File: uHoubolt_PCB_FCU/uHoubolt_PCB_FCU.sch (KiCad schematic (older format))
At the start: 0 parts

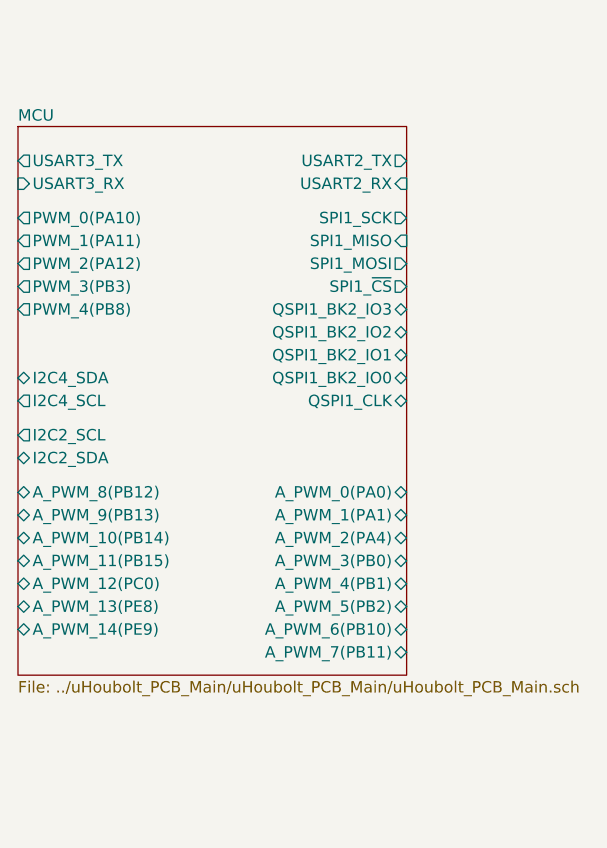
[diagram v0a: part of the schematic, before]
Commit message: add power symbols
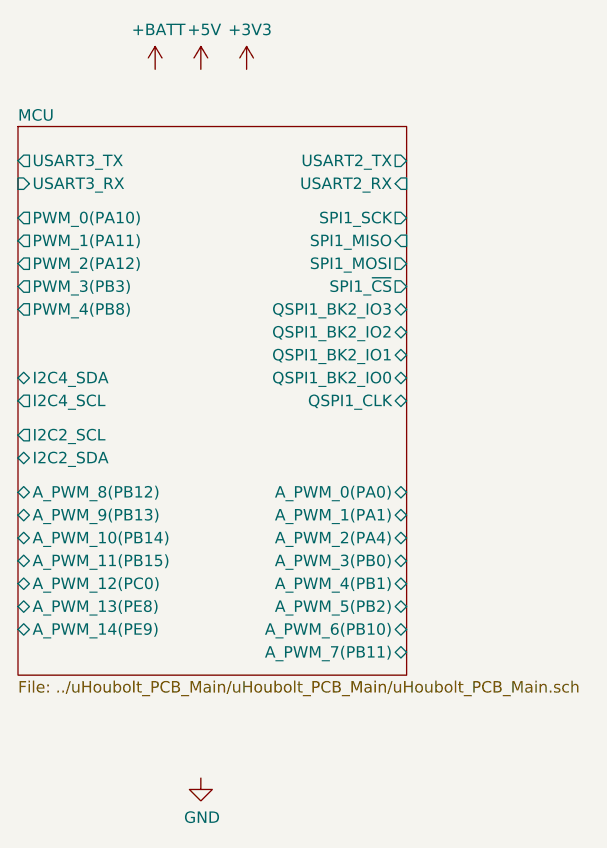
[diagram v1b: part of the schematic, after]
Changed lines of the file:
@@
 F38 "PWM_4(PB8)" O L 4050 3300 50
 $EndSheet
+$Comp
+L power:+BATT #PWR?
+U 1 1 5FDDCBBE
+P 4650 2250
+F 0 "#PWR?" H 4650 2100 50  0001 C CNN
+F 1 "+BATT" H 4665 2423 50  0000 C CNN
+F 2 "" H 4650 2250 50  0001 C CNN
+F 3 "" H 4650 2250 50  0001 C CNN
+	1    4650 2250
+	1    0    0    -1
+$EndComp
+$Comp
+L power:+5V #PWR?
+U 1 1 5FDDCF04
+P 4850 2250
+F 0 "#PWR?" H 4850 2100 50  0001 C CNN
+F 1 "+5V" H 4865 2423 50  0000 C CNN
+F 2 "" H 4850 2250 50  0001 C CNN
+F 3 "" H 4850 2250 50  0001 C CNN
+	1    4850 2250
+	1    0    0    -1
+$EndComp
+$Comp
+L power:+3V3 #PWR?
+U 1 1 5FDDD390
+P 5050 2250
+F 0 "#PWR?" H 5050 2100 50  0001 C CNN
+F 1 "+3V3" H 5065 2423 50  0000 C CNN
+F 2 "" H 5050 2250 50  0001 C CNN
+F 3 "" H 5050 2250 50  0001 C CNN
+	1    5050 2250
+	1    0    0    -1
+$EndComp
+$Comp
+L power:GND #PWR?
+U 1 1 5FDDDF58
+P 4850 5350
+F 0 "#PWR?" H 4850 5100 50  0001 C CNN
+F 1 "GND" H 4855 5177 50  0000 C CNN
+F 2 "" H 4850 5350 50  0001 C CNN
+F 3 "" H 4850 5350 50  0001 C CNN
+	1    4850 5350
+	1    0    0    -1
+$EndComp
 $EndSCHEMATC

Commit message: add 10A solenoid circuit
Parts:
- added C1, C?: 0.1u, symbol Device:C_Small
- added J1, J?: 206832-0202, symbol Connector_Generic:Conn_01x02
- added Q1, Q?: BUK9M15-40H, Package_TO_SOT_SMD:LFPAK33, symbol Transistor_FET:BUK9M15-60EX
- added R1, R?: shunt, symbol Device:R_Small
- added R2, R?: 20k, symbol Device:R_Small
- added R3, R?: 200, symbol Device:R_Small
- added U1, U?: INA180, Package_TO_SOT_SMD:SOT-23-6, symbol TXV_LIB:INA180
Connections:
- net labels added: SOLCONTROL1, SOLCONTROL2, SOLSENSE1, SOLSENSE2
- wire segments 0 -> 56

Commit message: add 5V Zünder circuit
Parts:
- removed Q1, Q?: BUK9M15-40H, Package_TO_SOT_SMD:LFPAK33, symbol Transistor_FET:BUK9M15-60EX
- added C3, C4: 0.1u, symbol Device:C_Small
- added J3, J4: 206832-0202, symbol Connector_Generic:Conn_01x02
- added Q1, Q2, Q3, Q4: BSB008NE2LX, Package_DirectFET:DirectFET_MX, symbol Transistor_FET:BSB008NE2LX
- added R10, R7: shunt, symbol Device:R_Small
- added R11, R8: 20k, symbol Device:R_Small
- added R12, R9: 200, symbol Device:R_Small
- added U3, U4: INA180, Package_TO_SOT_SMD:SOT-23-6, symbol TXV_LIB:INA180
- gave numbers to parts that had none: 6
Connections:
- net labels added: SERVOCONTROL1, SERVOCONTROL2, SERVOSENSE1, SERVOSENSE2
- wire segments 56 -> 112
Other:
- moved on the sheet: C1, C2, J1, J2, R1, R2, R3, R4, R5, R6, U1, U2

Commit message: add continuity sense to 5V Zünder circuit
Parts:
- added R13: 20k, symbol Device:R_Small
- added R14: 200, symbol Device:R_Small
- added R15: 560k, symbol Device:R_Small
- added R16: 2.0M, symbol Device:R_Small
- R10: value shunt -> 560k
- R11: value 20k -> 2.0M
- R12: value 200 -> shunt
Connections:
- net GND: now also R12.2, R13.1, R15.2; no longer R11.1
- net at J3.2 (Pin_2), Q3.1 (D): now also R11.1
- net at Q4.2 (G): now also R14.2; no longer R12.2
- net at Q4.3 (S), U4.3 (+): now also R12.1; no longer R10.1
- net at J4.2 (Pin_2), Q4.1 (D): now also R16.1
- net SERVOCONTROL1 renamed IGNITECONTROL1
- net SERVOCONTROL2 renamed IGNITECONTINUITY1
- net IGNITECONTINUITY1: now also R10.1; no longer R12.1
- net SERVOSENSE1 renamed IGNITESENSE1
- net SERVOSENSE2 renamed IGNITESENSE2
- new net IGNITECONTINUITY2: R15.1, R16.2
- new net IGNITECONTROL2: R13.2, R14.1
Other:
- moved on the sheet: J3, R8, R9

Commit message: add 2x variable input pressure sensor circuit
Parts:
- added C? (x2): 0.1u, symbol Device:C_Small
- added J? (x2): JST GH, symbol Connector_Generic_MountingPin:Conn_01x04_MountingPin
- added JP?: SolderJumper_3_Open, symbol Jumper:SolderJumper_3_Open
- added R?: 3.3k, symbol Device:R_Small
- added R?: 6.8k, symbol Device:R_Small
- added R? (x2): 3.3k/0, symbol Device:R_Small
- added R? (x2): 6.8k/160, symbol Device:R_Small
- added U? (x2): INA180, Package_TO_SOT_SMD:SOT-23-6, symbol TXV_LIB:INA180
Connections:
- net +3V3: now also C1.1, C2.1, C3.1, C4.1, U1.6 (V+), U2.6 (V+), U3.6 (V+), U4.6 (V+), C?.1, C?.1, U?.6 (V+), U?.6 (V+)
- net +5V: now also JP?.1 (A), R?.1; no longer C1.1, C2.1, C3.1, C4.1, U1.6 (V+), U2.6 (V+), U3.6 (V+), U4.6 (V+)
- net +BATT: now also JP?.3 (B)
- net GND: now also C?.2, C?.2, J?.4 (Pin_4), J?.4 (Pin_4), J?.MP (MountPin), J?.MP (MountPin), R?.2, R?.2, R?.2, U?.2 (GND), U?.2 (GND)
- new net: J?.1 (Pin_1), JP?.2 (C)
- new net: J?.2 (Pin_2), R?.1, U?.3 (+) (x2)
- new net: J?.3 (Pin_3), U?.4 (-) (x2)
- new net PRESSURESENSE2: R?.1, R?.2, U?.1
- new net SUPPLYMEASURE: R?.1, R?.2
- new net TESTPRESSURESENSE1: R?.1, R?.2, U?.1
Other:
- note added: "Vdrive - pyro voltage from PMU\n"
- note added: "op-amp for diff. 150mV bridge input,\nvoltage div. for 0-5V or 4-20mA input.\n(3.3k/6.8k for 0-5V,\n0/160 Ohm for 4-20mA)"
- moved on the sheet: C3, C4, J3, J4, Q3, Q4, R10, R11, R12, R13, R14, R15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

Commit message: Added modules from Trello list. Todo: Review, assign pins to labels, component naming.
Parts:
- removed C4, C?: 0.1u, symbol Device:C_Small
- removed J4: 206832-0202, symbol Connector_Generic:Conn_01x02
- removed J?: JST GH, symbol Connector_Generic_MountingPin:Conn_01x04_MountingPin
- removed Q4: BSB008NE2LX, Package_DirectFET:DirectFET_MX, symbol Transistor_FET:BSB008NE2LX
- removed R12, R4, R7: shunt, symbol Device:R_Small
- removed R13: 20k, symbol Device:R_Small
- removed R14: 200, symbol Device:R_Small
- removed R15: 560k, symbol Device:R_Small
- removed R16: 2.0M, symbol Device:R_Small
- removed R?: 3.3k/0, symbol Device:R_Small
- removed R?: 6.8k/160, symbol Device:R_Small
- removed U4, U?: INA180, Package_TO_SOT_SMD:SOT-23-6, symbol TXV_LIB:INA180
- added C? (x6): 0.1u, symbol Device:C_Small
- added C? (x2): 1u, symbol Device:C_Small
- added C? (x2): 22p, symbol Device:C_Small
- added C? (x2): 100n, symbol Device:C_Small
- added C?: 120n, symbol Device:C_Small
- added C?: 6.8n, symbol Device:C_Small
- added C?: 4.7u, symbol Device:C_Small
- added C? (x5): 33u, symbol Device:C_Small
- added C?: C_Small, symbol Device:C_Small
- added C? (x4): 100u, symbol Device:C_Small
- added F? (x3): Polyfuse, symbol Device:Polyfuse
- added J? (x7): JST GH, symbol Connector_Generic_MountingPin:Conn_01x04_MountingPin
- added J? (x3): JST GH, symbol Connector_Generic:Conn_01x02
- added J? (x2): 206832-0202, symbol Connector_Generic:Conn_01x02
- added JP?: SolderJumper_3_Open, symbol Jumper:SolderJumper_3_Open
- added L?: 1.5m, symbol Device:L_Small
- added Q? (x2): BSB008NE2LX, Package_DirectFET:DirectFET_MX, symbol Transistor_FET:BSB008NE2LX
- added R?: 3.3k/0, symbol Device:R_Small
- added R?: 6.8k/160, symbol Device:R_Small
- added R? (x3): 1k, symbol Device:R_Small
- added R?: 115k, symbol Device:R_Small
- added R? (x5): 20k, symbol Device:R_Small
- added R? (x6): 10k, symbol Device:R_Small
- added R? (x4): 5m 1W, symbol Device:R_Small
- added R? (x6): 47k, symbol Device:R_Small
- added R? (x6): 33k, symbol Device:R_Small
- added R?: 51k, symbol Device:R_Small
- added R? (x2): 200, symbol Device:R_Small
- added R? (x2): 200k, symbol Device:R_Small
- added R? (x2): 56k, symbol Device:R_Small
- added R?: 499k, symbol Device:R_Small
- added R?: R_Small, symbol Device:R_Small
- added U? (x6): INA180, Package_TO_SOT_SMD:SOT-23-6, symbol TXV_LIB:INA180
- added U?: BNO055, Package_LGA:LGA-28_5.2x3.8mm_P0.5mm, symbol Sensor_Motion:BNO055
- added U? (x3): AD8426, symbol SCB-rescue:AD8426-TXV_Library_Symbols
- added U?: SIC431CED-T1-GE3, symbol TXV_LIB:SIC431CED-T1-GE3
- added Y?: 32.768kHz, symbol Device:Crystal_Small
- R1: value shunt -> 5m 1W; Type (none) -> ULR1S-R005FT2
- R10: value 560k -> 56k
- R11: value 2.0M -> 200k
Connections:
- net +3V3: now also C?.1, C?.1, C?.1, C?.1, C?.1, C?.1, C?.2, C?.2, C?.2, J?.1 (Pin_1), J?.1 (Pin_1), J?.1 (Pin_1), R?.2, R?.2, R?.2, R?.2, R?.2, U?.28 (VDDIO), U?.3 (VDD), U?.5 (PS1), U?.6 (V+), U?.6 (V+), U?.6 (V+), U?.6 (V+), U?.6 (V+), U?.6 (V+)
- net +5V: now also J?.1 (Pin_1), J?.1 (Pin_1), J?.1 (Pin_1), JP?.1 (A)
- net +BATT: now also JP?.3 (B); no longer J3.1 (Pin_1)
- net GND: now also C?.1, C?.1, C?.1, C?.1, C?.1, C?.1, C?.1, C?.1, C?.2, C?.2, C?.2, C?.2, C?.2, C?.2, C?.2, J?.4 (Pin_4), J?.4 (Pin_4), J?.4 (Pin_4), J?.4 (Pin_4), J?.4 (Pin_4), J?.4 (Pin_4), J?.4 (Pin_4), J?.MP (MountPin), J?.MP (MountPin), J?.MP (MountPin), J?.MP (MountPin), J?.MP (MountPin), J?.MP (MountPin), J?.MP (MountPin), R?.1, R?.1, R?.1, R?.1, R?.1, R?.1, R?.1, R?.1, R?.1, R?.1, R?.1, R?.2, R?.2, R?.2, R?.2, R?.2, R?.2, R?.2, R?.2, R?.2, R?.2, U?.12 (-IN2), U?.12 (-IN2), U?.12 (-IN2), U?.13 (-Vs), U?.13 (-Vs), U?.13 (-Vs), U?.15 (GNDIO), U?.16 (GNDIO), U?.17 (COM3), U?.18 (COM2), U?.2 (GND), U?.2 (GND), U?.2 (GND), U?.2 (GND), U?.2 (GND), U?.2 (GND), U?.2 (GND), U?.25 (GNDIO), U?.4 (-), U?.4 (-), U?.6 (PS0), U?.6 (REF1), U?.6 (REF1), U?.6 (REF1), U?.7 (REF2), U?.7 (REF2), U?.7 (REF2), U?.8 (-Vs), U?.8 (-Vs), U?.8 (-Vs)
- net IGNITECONTINUITY1: now also R?.1, R?.1, R?.2, R?.2
- net IGNITECONTROL1: now also R?.1, R?.1, R?.2, R?.2
- net IGNITESENSE1: now also U?.1, U?.1
- net PRESSURESENSE2: now also U?.1
- net Vdrive: now also C?.1, C?.1, C?.2, F?.2, F?.2, F?.2, R?.1, R?.1, R?.1, U?.1 (V_IN), U?.2 (V_IN), U?.22 (V_IN), U?.26 (V_IN_PAD)
- net at Q2.3 (S), U2.3 (+): now also R?.1
- net at Q3.3 (S), U3.3 (+): now also R?.1
- new net: F?.1, J3.1 (Pin_1)
- new net: J?.1 (Pin_1), JP?.2 (C)
- new net: J?.2 (Pin_2), R?.1, U?.3 (+)
- new net: J?.3 (Pin_3), U?.4 (-) (x4)
- new net: J?.2 (Pin_2), U?.3 (+) (x3)
- new net: J?.1 (Pin_1), U?.1 (-IN1), U?.9 (+IN2) (x3)
- new net: C?.2, U?.26 (XOUT32), Y?.1
- new net: C?.2, U?.27 (XIN32), Y?.2
- new net: R?.1, U?.4 (~BOOT_LOAD_PIN)
- new net: C?.1, U?.9 (CAP)
- new net: R?.1, R?.2, U?.17 (FB)
- new net: R?.2, U?.14 (OUT2) (x3)
- new net: R?.2, U?.15 (OUT1) (x3)
- new net: C?.1, R?.1, R?.2, U?.16 (A_GND)
- new net: Q?.3 (S), R?.1, U?.3 (+) (x2)
- new net: L?.1, U?.5 (SW), U?.6 (SW), U?.7 (SW), U?.8 (SW), U?.9 (SW)
- new net: C?.1, U?.12 (VDRV)
- new net: C?.1, C?.2, C?.2, C?.2, C?.2, C?.2, C?.2, U?.13 (P_GND), U?.27 (P_GND_PAD), U?.3 (P_GND), U?.4 (P_GND)
- new net: C?.2, R?.1, U?.15 (VDD)
- new net: R?.1, U?.20 (MODE2)
- new net: R?.2, U?.21 (MODE1)
- new net: C?.1, U?.23 (BOOT)
- new net: R?.1, U?.24 (PHASE)
- new net: C?.2, U?.25 (A_GND_PAD)
- new net: J?.2 (Pin_2), Q?.1 (D), R?.1 (x2)
- new net: Q?.2 (G), R?.2 (x2)
- new net: F?.1, J?.1 (Pin_1) (x2)
- new net: C?.2, R?.2
- new net +7.5V: C?.1, C?.1, C?.1, C?.1, J?.3 (Pin_3), J?.3 (Pin_3), J?.3 (Pin_3), L?.2, R?.2, U?.16 (+Vs), U?.16 (+Vs), U?.16 (+Vs), U?.18 (V_OUT), U?.4 (+IN1), U?.4 (+IN1), U?.4 (+IN1), U?.5 (+Vs), U?.5 (+Vs), U?.5 (+Vs)
- new net BNO_INT: U?.14 (INT)
- new net BNO_RESET: R?.1, U?.11 (~RESET)
- new net BNO_RX: U?.19 (COM1)
- new net BNO_TX: U?.20 (COM0)
- new net PRESSURESENSE1: U?.1
- new net PRESSURESENSE3: U?.1
- new net SERVO1_FDBK_GND: R?.1, R?.2
- new net SERVO1_FDBK_PWR: R?.1, R?.2
- new net SERVO1_PWM: J?.2 (Pin_2), R?.2
- new net SERVO2_FDBK_GND: R?.1, R?.2
- new net SERVO2_FDBK_PWR: R?.1, R?.2
- new net SERVO2_PWM: J?.2 (Pin_2), R?.2
- new net SERVO3_FDBK_GND: R?.1, R?.2
- new net SERVO3_FDBK_PWR: R?.1, R?.2
- new net SERVO3_PWM: J?.2 (Pin_2), R?.2
- new net TEMP1: C?.2, J?.2 (Pin_2), R?.1
- new net TEMP2: C?.2, J?.2 (Pin_2), R?.1
- new net TEMP3: C?.2, J?.2 (Pin_2), R?.1
- new net TESTPRESSURESENSE2: R?.1, R?.2, U?.1
- new net VOLTREG_EN: U?.19 (EN)
- no-connect marks 0 -> 16
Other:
- note added: "12V"
- note added: "5V SENSING"
- note added: "7.4V Voltage Reg"
- note added: "FDBK"
- note added: "GND"
- note added: "IMU"
- note added: "NTC: TG250J34GBNR, 5k Ohm\nhttps://www.mouser.at/datasheet/2/18/Amphenol_2017.06.15_Datasheet_CIG_thermistor-1730609.pdf"
- note added: "NTCs"
- note added: "PRESSURE GROUND TESTING"
- note added: "PRESSURE SENSING"
- note added: "PWM"
- note added: "PWR\n"
- note added: "PYRO/IGNITION"
- note added: "SERVOs"
- note added: "SOLENOIDS"
- moved on the sheet: C1, C2, C3, C?, J1, J2, J3, J?, JP?, Q1, Q2, Q3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

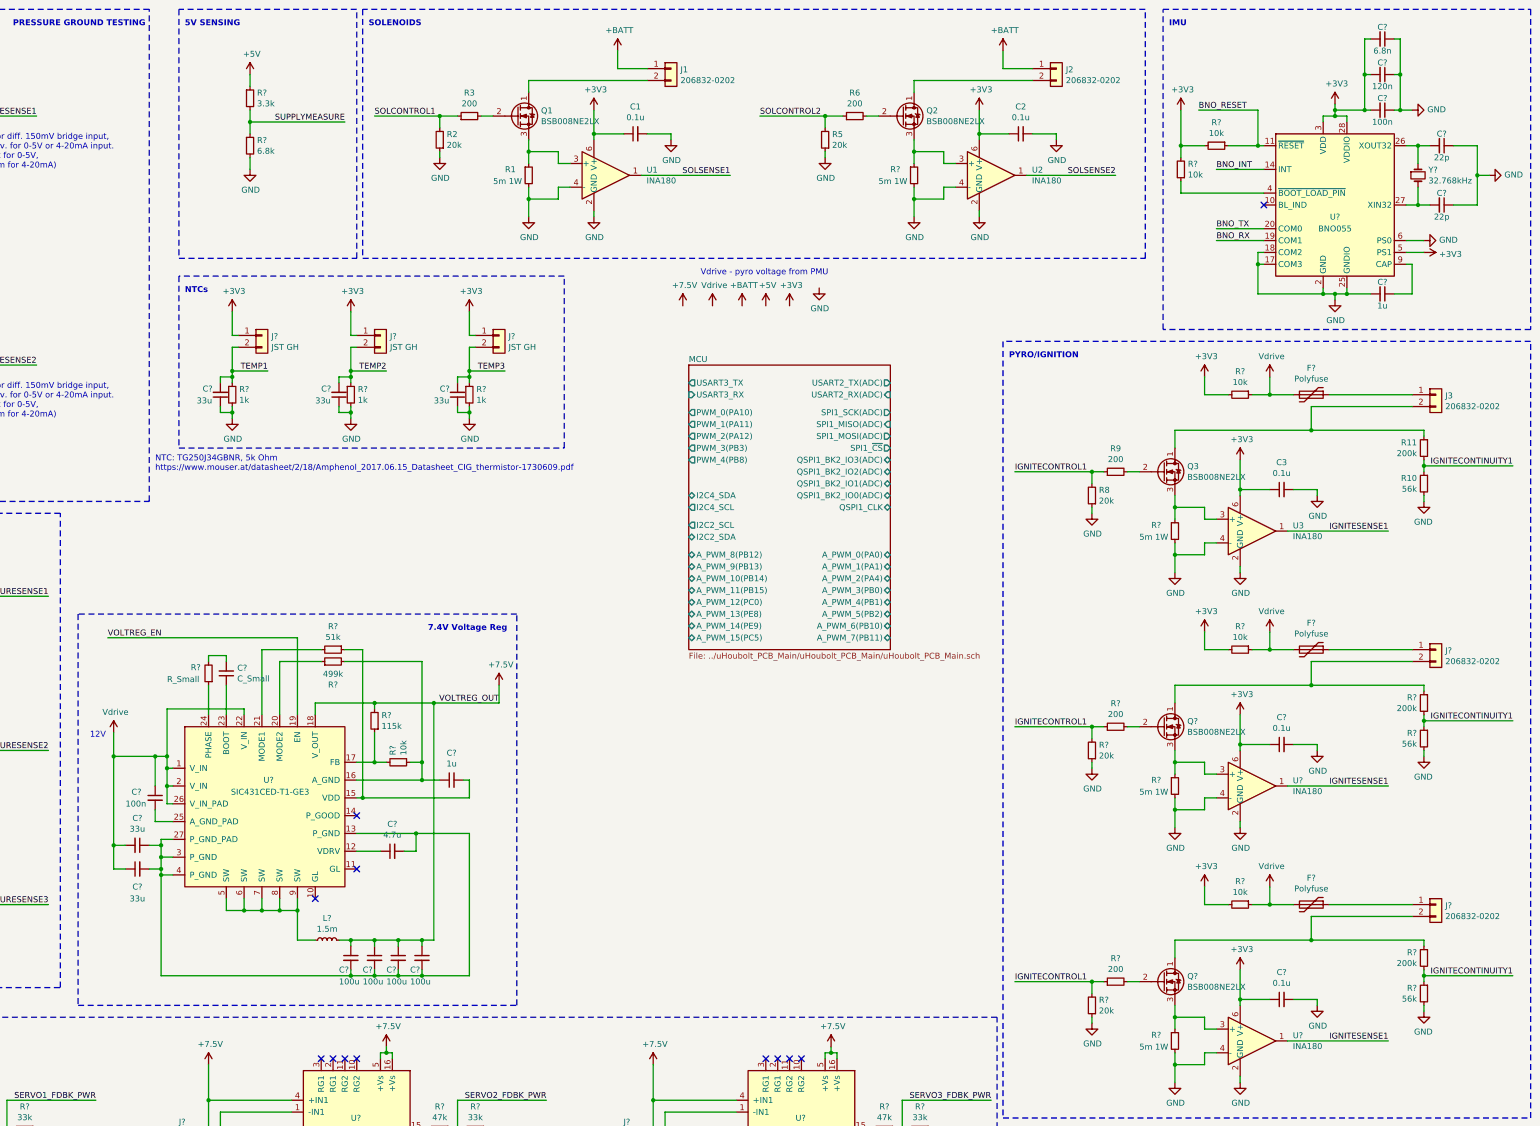
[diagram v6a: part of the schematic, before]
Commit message: Changed IMU and assigned sigs to uC pins.
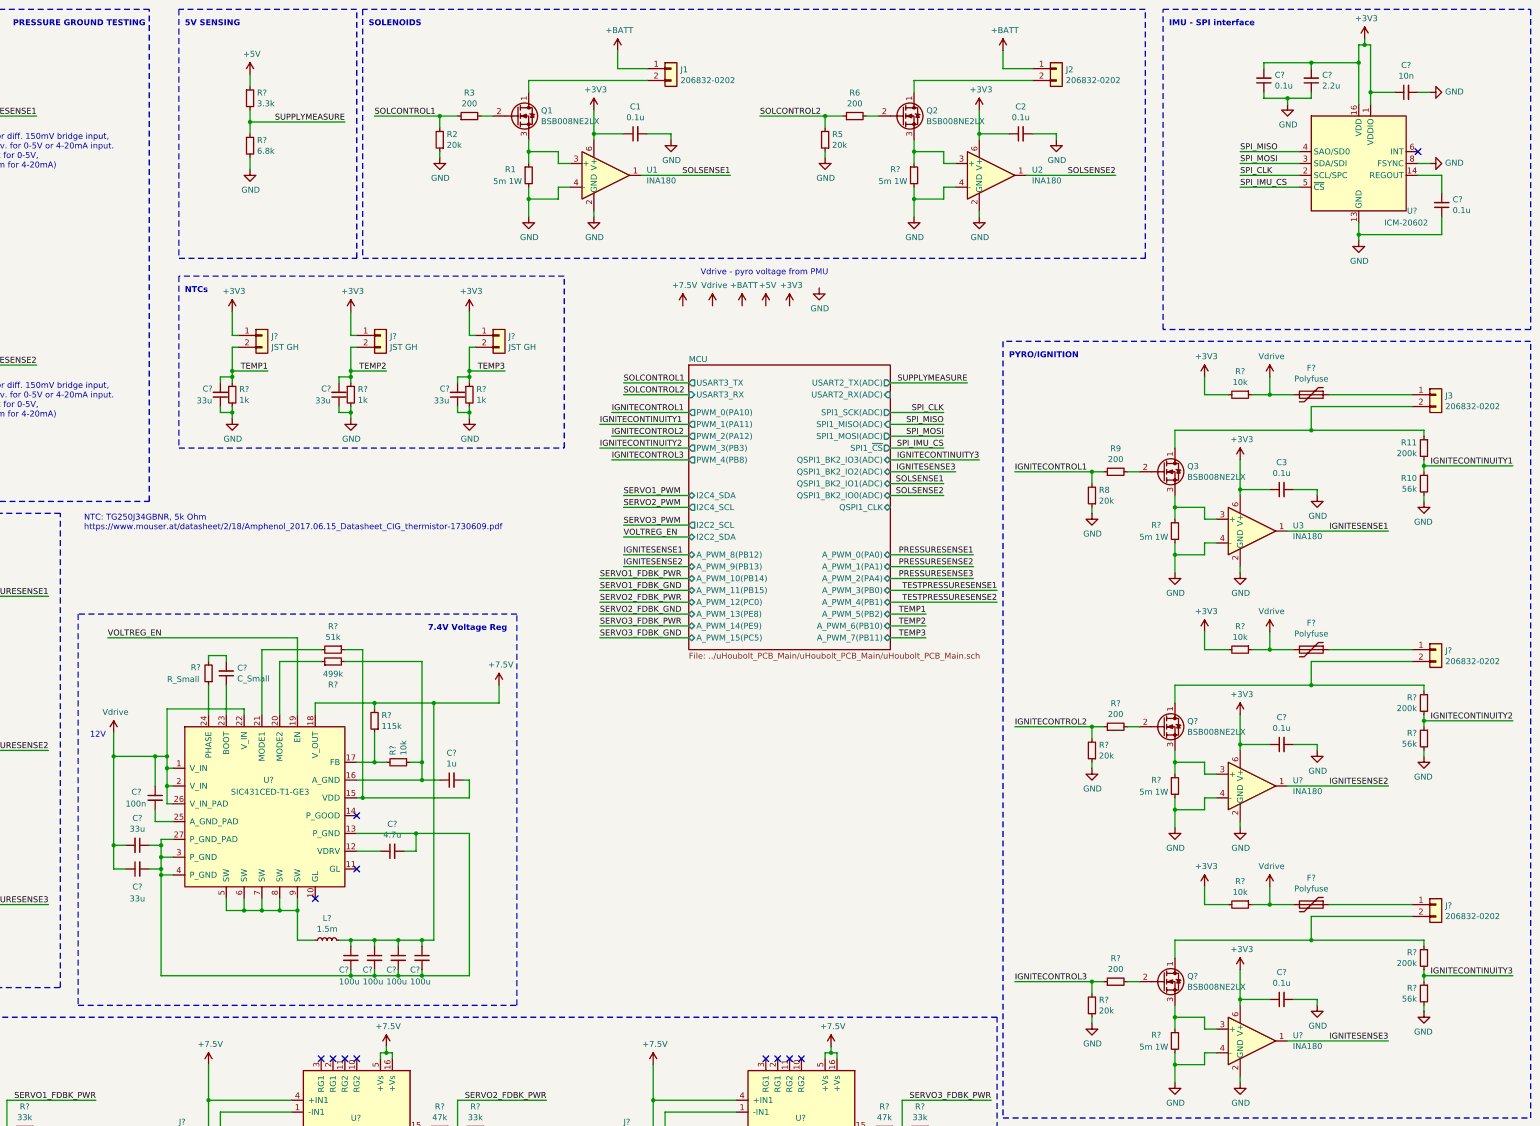
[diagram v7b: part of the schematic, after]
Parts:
- removed C?: 1u, symbol Device:C_Small
- removed C? (x2): 22p, symbol Device:C_Small
- removed C?: 100n, symbol Device:C_Small
- removed C?: 120n, symbol Device:C_Small
- removed C?: 6.8n, symbol Device:C_Small
- removed R? (x2): 10k, symbol Device:R_Small
- removed U?: BNO055, Package_LGA:LGA-28_5.2x3.8mm_P0.5mm, symbol Sensor_Motion:BNO055
- removed Y?: 32.768kHz, symbol Device:Crystal_Small
- added C?: 10n, symbol Device:C_Small
- added C?: 2.2u, symbol Device:C_Small
- added C? (x2): 0.1u, symbol Device:C_Small
- added U?: ICM-20602, Package_LGA:LGA-16_3x3mm_P0.5mm_LayoutBorder3x5y, symbol Sensor_Motion:ICM-20602
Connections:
- net +3V3: now also C?.1, C?.2, C?.2, U?.1 (VDDIO), U?.16 (VDD)
- net GND: now also C?.1, C?.1, C?.1, C?.2, U?.10 (GND), U?.11 (GND), U?.12 (GND), U?.13 (GND), U?.15 (GND), U?.8 (FSYNC), U?.9 (GND)
- net IGNITECONTINUITY1: no longer R?.1, R?.1, R?.2, R?.2
- net IGNITECONTROL1: no longer R?.1, R?.1, R?.2, R?.2
- net IGNITESENSE1: no longer U?.1, U?.1
- new net: C?.2, U?.14 (REGOUT)
- new net IGNITECONTINUITY2: R?.1, R?.2
- new net IGNITECONTINUITY3: R?.1, R?.2
- new net IGNITECONTROL2: R?.1, R?.2
- new net IGNITECONTROL3: R?.1, R?.2
- new net IGNITESENSE2: U?.1
- new net IGNITESENSE3: U?.1
- new net SPI_CLK: U?.2 (SCL/SPC)
- new net SPI_IMU_CS: U?.5 (~CS)
- new net SPI_MISO: U?.4 (SAO/SD0)
- new net SPI_MOSI: U?.3 (SDA/SDI)
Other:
- note added: "IMU - SPI interface"
- note removed: "IMU"
